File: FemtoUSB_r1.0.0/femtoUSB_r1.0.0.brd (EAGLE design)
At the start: 20.7 x 15.2 mm, 25 parts, among them IC1 ATSAMD21E18A-MUT

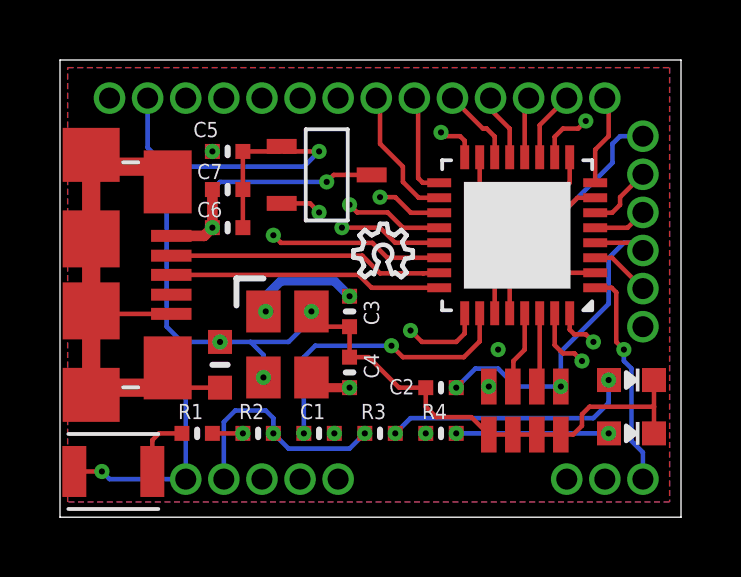
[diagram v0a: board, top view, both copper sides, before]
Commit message: Corrected the Make and model of the LDO Voltage Regulator. Board now powers on.
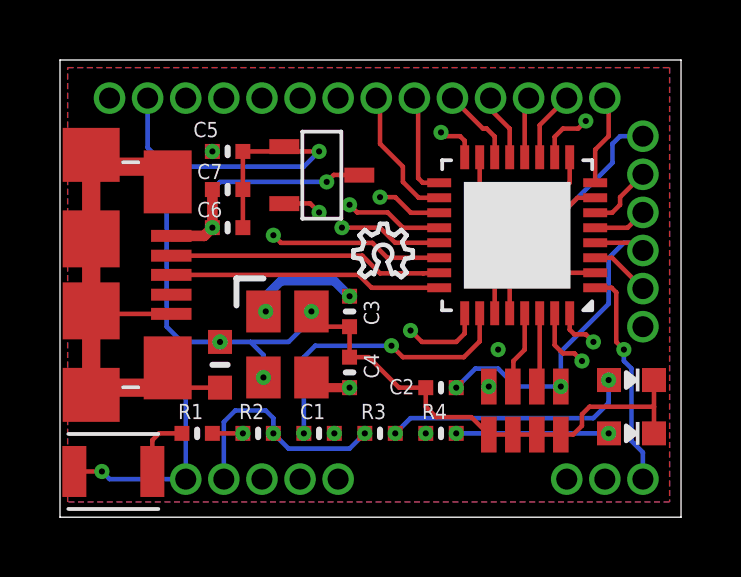
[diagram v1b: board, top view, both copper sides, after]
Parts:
- LDO_VREG: value LM3480 -> MCP1700T-3302E/TT; device ti-lm3480:LM3480 -> MCP1700T-3302E_TT:MCP1700T-3302E/TT
- moved LDO_VREG 1.64 mm to (8.08, 12.9)
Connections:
- net 3.3V: now also LDO_VREG.VOUT; no longer LDO_VREG.P$2
- net GND: now also LDO_VREG.GND; no longer LDO_VREG.P$1
- net VIN: now also LDO_VREG.VIN; no longer LDO_VREG.P$3
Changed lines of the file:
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@@
 <setting verticaltext="up"/>
 </settings>
-<grid distance="10" unitdist="mil" unit="mil" style="lines" multiple="1" display="yes" altdistance="0.025" altunitdist="inch" altunit="inch"/>
+<grid distance="1" unitdist="mil" unit="mil" style="lines" multiple="1" display="yes" altdistance="0.025" altunitdist="inch" altunit="inch"/>
 <layers>
 <layer number="1" name="Top" color="4" fill="1" visible="yes" active="yes"/>
@@
 <attribute name="DIGIKEY_PART" value="TSX-3225 32.0000MF15X-B-ND" x="8.382" y="6.858" size="1.778" layer="27" rot="R270" display="off"/>
 </element>
-<element name="LDO_VREG" library="ti-lm3480" package="LM3480" value="LM3480" x="8.89" y="11.43" rot="R270"/>
+<element name="LDO_VREG" library="MCP1700T-3302E_TT" package="MCP1700T-3302E/TT" value="MCP1700T-3302E/TT" x="8.0772" y="12.8524" rot="R270"/>
 <element name="C5" library="microbuilder" package="_0402MP" value="2.2uF" x="5.588" y="12.192" smashed="yes">
 <attribute name="NAME" x="4.445" y="12.6683" size="0.508" layer="25" font="vector" ratio="20"/>
@@
 <contactref element="C4" pad="1"/>
 <contactref element="LED1" pad="C"/>
-<contactref element="LDO_VREG" pad="P$1"/>
+<contactref element="LDO_VREG" pad="GND"/>
 <contactref element="C5" pad="2"/>
 <contactref element="C6" pad="2"/>
@@
 <wire x1="6.096" y1="12.192" x2="6.096" y2="10.922" width="0.1524" layer="1"/>
 <wire x1="6.096" y1="12.192" x2="7.304" y2="12.192" width="0.1524" layer="1"/>
-<wire x1="7.304" y1="12.192" x2="7.39" y2="12.36" width="0.1524" layer="1"/>
+<wire x1="7.304" y1="12.192" x2="7.4772" y2="12.3524" width="0.1524" layer="1"/>
 <wire x1="2.921" y1="13.97" x2="2.921" y2="12.319" width="0.1524" layer="16"/>
 <wire x1="2.921" y1="12.319" x2="3.556" y2="11.684" width="0.1524" layer="16"/>
@@
 <via x="8.636" y="12.192" extent="1-16" drill="0.2032" diameter="0.508"/>
 <wire x1="8.636" y1="12.192" x2="7.476" y2="12.192" width="0.1524" layer="1"/>
-<wire x1="7.476" y1="12.192" x2="7.39" y2="12.36" width="0.1524" layer="1"/>
+<wire x1="7.476" y1="12.192" x2="7.4772" y2="12.3524" width="0.1524" layer="1"/>
 <wire x1="0.478" y1="1.524" x2="1.397" y2="1.524" width="0.1524" layer="1"/>
 <via x="1.397" y="1.524" extent="1-16" drill="0.2032" diameter="0.508"/>
@@
 <contactref element="C5" pad="1"/>
 <contactref element="R3" pad="1"/>
-<contactref element="LDO_VREG" pad="P$2"/>
+<contactref element="LDO_VREG" pad="VOUT"/>
 <via x="5.08" y="12.192" extent="1-16" drill="0.2032" diameter="0.508"/>
 <wire x1="5.08" y1="12.192" x2="4.318" y2="12.954" width="0.1524" layer="15"/>
@@
 <wire x1="6.096" y1="9.652" x2="7.112" y2="10.668" width="0.1524" layer="15"/>
 <via x="10.16" y="2.794" extent="1-16" drill="0.2032" diameter="0.508"/>
-<wire x1="7.39" y1="10.46" x2="8.336" y2="10.46" width="0.1524" layer="1"/>
+<wire x1="7.4772" y1="10.4524" x2="8.336" y2="10.46" width="0.1524" layer="1"/>
 <wire x1="8.336" y1="10.46" x2="8.636" y2="10.16" width="0.1524" layer="1"/>
 <wire x1="7.112" y1="2.794" x2="7.62" y2="2.286" width="0.1524" layer="16"/>
@@
 <wire x1="1.524" y1="12.446" x2="1.524" y2="13.843" width="0.1524" layer="15"/>
 <wire x1="1.524" y1="13.843" x2="1.651" y2="13.97" width="0.1524" layer="15"/>
-<contactref element="LDO_VREG" pad="P$3"/>
+<contactref element="LDO_VREG" pad="VIN"/>
 <contactref element="C6" pad="1"/>
 <contactref element="C7" pad="1"/>
@@
 <wire x1="5.334" y1="11.176" x2="5.08" y2="10.922" width="0.1524" layer="16"/>
 <wire x1="5.08" y1="10.922" x2="5.08" y2="9.652" width="0.1524" layer="16"/>
-<wire x1="10.39" y1="11.41" x2="9.124" y2="11.41" width="0.1524" layer="1"/>
+<wire x1="9.9772" y1="11.4024" x2="9.124" y2="11.41" width="0.1524" layer="1"/>
 <wire x1="9.124" y1="11.41" x2="8.89" y2="11.176" width="0.1524" layer="1"/>
 </signal>

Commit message: Updating the QFN (no leads) chip version of the board - adding in missing 10uF caps and 10uH inductor
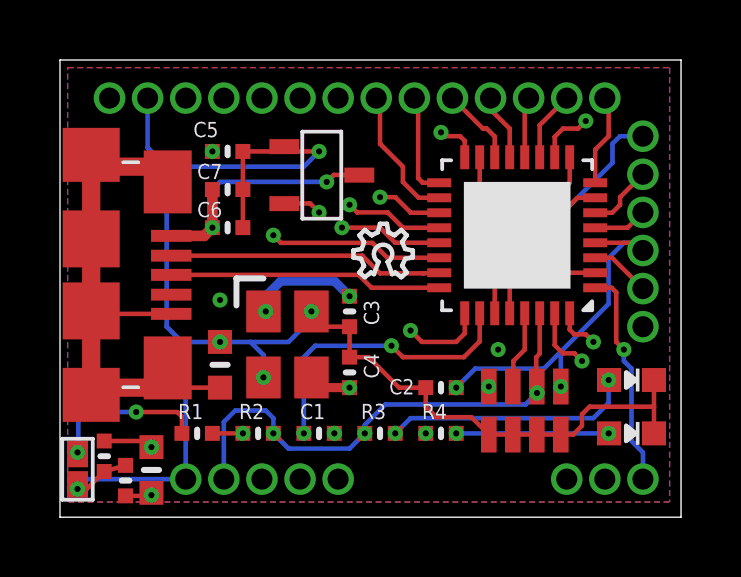
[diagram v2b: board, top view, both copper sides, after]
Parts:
- added C8, C9: 10uF, microbuilder:_0402MP
- added L1: 10uH, microbuilder:_0603MP
- BTN: device omron_tactile_switch:SIDE_ACT_NO_GND_NO_BOSS -> femtoduino:SPST_SMD
- moved BTN 1.20 mm to (0.58, 1.60), turned to 270 degrees
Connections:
- removed net VDDIN: C_ARR1.5, IC1.30
- net 3.3V: now also C8.2, C_ARR1.5, IC1.30, L1.1
- net GND: now also C8.1, C9.1
- net VDDANA: now also C9.2, L1.2
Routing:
- net 3.3V: track 25.1 -> 40.0 mm, vias 4 -> 7
- net VDDANA: track 9.06 -> 23.8 mm, vias 2 -> 3
- net N$26: track 2.12 -> 5.30 mm, vias 0 -> 2
- net VDDIN: track 2.48 -> 0.00 mm
- net GND: track 70.4 -> 72.4 mm
- net PA28: track 11.2 -> 12.3 mm

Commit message: Updating r1.x version of FemtoUSB (QFN and QFP chip version). Pin PA15 and GND pads now available to start board up in bootloader mode (SAM-BA)
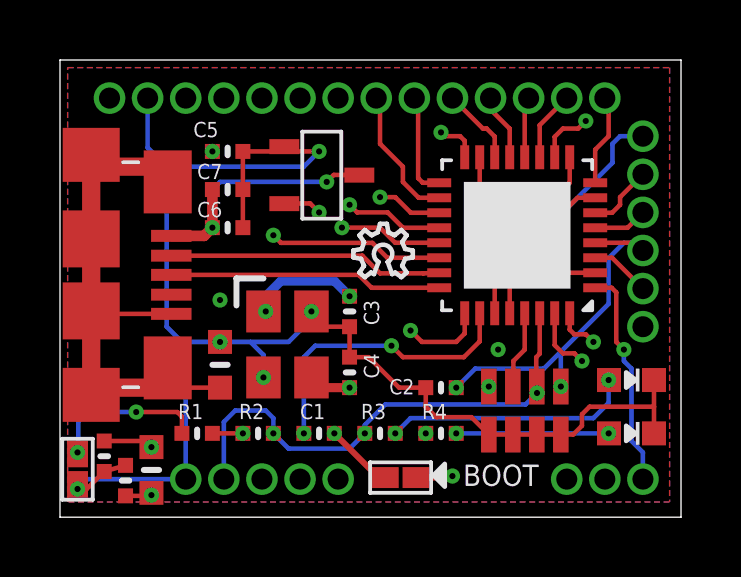
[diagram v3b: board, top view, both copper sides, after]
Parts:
- added U$38: SPST_SMD, femtoduino:SPST_SMD
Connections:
- net GND: now also U$38.2
- net PA15/XOUT: now also U$38.1
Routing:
- net PA15/XOUT: track 13.1 -> 21.7 mm, vias 2 -> 3
- net GND: track 72.4 -> 74.7 mm
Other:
- board text added: "BOOT"
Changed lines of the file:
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@@
 <setting verticaltext="up"/>
 </settings>
-<grid distance="1" unitdist="mil" unit="mil" style="lines" multiple="1" display="yes" altdistance="0.025" altunitdist="inch" altunit="inch"/>
+<grid distance="5" unitdist="mil" unit="mil" style="lines" multiple="1" display="yes" altdistance="0.025" altunitdist="inch" altunit="inch"/>
 <layers>
 <layer number="1" name="Top" color="4" fill="1" visible="yes" active="yes"/>
@@
 <wire x1="0" y1="15.24" x2="0" y2="0" width="0" layer="20"/>
 <text x="3.429" y="4.826" size="0.7112" layer="26" font="vector" ratio="20" rot="MR90">FemtoUSB</text>
-<text x="2.159" y="5.715" size="0.7112" layer="26" font="vector" ratio="20" rot="MR90">r1.0.0</text>
+<text x="2.0828" y="6.6548" size="0.7112" layer="26" font="vector" ratio="20" rot="MR90">r1.0.0</text>
 <text x="0.762" y="3.175" size="0.7112" layer="26" font="vector" ratio="20" rot="MR90">femtoduino.com</text>
 <text x="2.032" y="13.081" size="0.7112" layer="26" font="vector" ratio="20" rot="SMR90" align="top-right">VIN</text>
@@
 <circle x="16.2814" y="6.5786" radius="0.250159375" width="0.254" layer="26"/>
 <circle x="16.2814" y="5.5626" radius="0.250159375" width="0.254" layer="26"/>
+<text x="13.4366" y="1.0414" size="0.7112" layer="25" font="vector" ratio="20">BOOT</text>
+<polygon width="0.1524" layer="25">
+<vertex x="12.827" y="1.778"/>
+<vertex x="12.446" y="1.397"/>
+<vertex x="12.827" y="1.016"/>
+</polygon>
 </plain>
 <attributes>
@@
 <element name="C9" library="microbuilder" package="_0402MP" value="10uF" x="1.4732" y="2.032" smashed="yes" rot="R90"/>
 <element name="C8" library="microbuilder" package="_0402MP" value="10uF" x="2.1844" y="1.2192" smashed="yes" rot="R270"/>
+<element name="U$38" library="femtoduino" package="SPST_SMD" value="SPST_SMD" x="11.3538" y="1.3208" rot="R180"/>
 </elements>
 <signals>
@@
 <wire x1="11.43" y1="7.874" x2="9.652" y2="6.096" width="0.1524" layer="15"/>
 <wire x1="9.652" y1="6.096" x2="9.652" y2="4.318" width="0.1524" layer="15"/>
+<contactref element="U$38" pad="1"/>
+<wire x1="11.8618" y1="1.3208" x2="13.0302" y2="1.3208" width="0.2032" layer="1"/>
+<wire x1="13.0302" y1="1.3208" x2="13.081" y2="1.3716" width="0.2032" layer="1"/>
+<via x="13.081" y="1.3716" extent="1-16" drill="0.2032" diameter="0.508"/>
+<wire x1="13.081" y1="1.3716" x2="13.6652" y2="1.3716" width="0.1524" layer="2"/>
+<wire x1="13.6652" y1="1.3716" x2="14.1478" y2="1.8542" width="0.1524" layer="2"/>
+<wire x1="14.1478" y1="1.8542" x2="14.1478" y2="2.9464" width="0.1524" layer="2"/>
+<wire x1="14.1478" y1="2.9464" x2="13.7922" y2="3.302" width="0.1524" layer="2"/>
+<wire x1="13.7922" y1="3.302" x2="10.668" y2="3.302" width="0.1524" layer="2"/>
+<wire x1="10.668" y1="3.302" x2="9.652" y2="4.318" width="0.1524" layer="2"/>
 </signal>
 <signal name="PA16/SERCOM1/PAD[0]/SPI/I2C">
@@
 <wire x1="12.192" y1="5.842" x2="12.192" y2="4.318" width="0.1524" layer="2"/>
 <wire x1="12.192" y1="4.318" x2="12.827" y2="3.683" width="0.1524" layer="2"/>
-<wire x1="12.827" y1="3.683" x2="13.462" y2="3.683" width="0.1524" layer="2"/>
-<wire x1="13.462" y1="3.683" x2="13.97" y2="3.175" width="0.1524" layer="2"/>
-<wire x1="13.97" y1="3.175" x2="14.986" y2="3.175" width="0.1524" layer="2"/>
-<wire x1="14.986" y1="3.175" x2="16.891" y2="1.27" width="0.1524" layer="2"/>
+<wire x1="12.827" y1="3.683" x2="14.478" y2="3.683" width="0.1524" layer="2"/>
+<wire x1="14.478" y1="3.683" x2="16.891" y2="1.27" width="0.1524" layer="2"/>
 </signal>
 <signal name="RESET">
@@
 <wire x1="0.889" y1="0.9398" x2="0.5842" y2="0.9398" width="0.1524" layer="1"/>
 <wire x1="1.4732" y1="1.524" x2="2.1844" y2="1.7272" width="0.1524" layer="1"/>
+<contactref element="U$38" pad="2"/>
+<wire x1="10.8458" y1="1.3208" x2="10.6172" y2="1.3208" width="0.2032" layer="1"/>
+<wire x1="10.6172" y1="1.3208" x2="9.144" y2="2.794" width="0.2032" layer="1"/>
 </signal>
 <signal name="3.3V">
@@
 <wire x1="3.048" y1="0.7366" x2="2.9464" y2="0.7112" width="0.1524" layer="1"/>
 <wire x1="2.9464" y1="0.7112" x2="2.1844" y2="0.7112" width="0.1524" layer="1"/>
+<wire x1="3.048" y1="0.7366" x2="3.048" y2="0.8128" width="0" layer="19" extent="1-2"/>
 </signal>
 <signal name="N$32">

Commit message: Updating gerbers and BoM/Partslist of QFN version
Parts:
- EPSON_TSX1: value 32MHz -> 48MHz
- LED1: value RED -> YELLOW
- LED2: value GREEN -> BLUE
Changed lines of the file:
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@@
 <attribute name="VALUE" x="8.001" y="2.0002" size="0.4572" layer="27" font="vector" ratio="20"/>
 </element>
-<element name="LED1" library="microbuilder" package="CHIPLED_0603_NOOUTLINE" value="RED" x="19.05" y="4.572" smashed="yes" rot="R270"/>
+<element name="LED1" library="microbuilder" package="CHIPLED_0603_NOOUTLINE" value="YELLOW" x="19.05" y="4.572" smashed="yes" rot="R270"/>
 <element name="R1" library="microbuilder" package="_0402MP" value="330" x="4.572" y="2.794" smashed="yes">
 <attribute name="NAME" x="3.937" y="3.2703" size="0.508" layer="25" font="vector" ratio="20"/>
@@
 <attribute name="NAME" x="10.1283" y="5.461" size="0.508" layer="25" font="vector" ratio="20" rot="R270"/>
 </element>
-<element name="LED2" library="microbuilder" package="CHIPLED_0603_NOOUTLINE" value="GREEN" x="19.05" y="2.794" smashed="yes" rot="R270"/>
+<element name="LED2" library="microbuilder" package="CHIPLED_0603_NOOUTLINE" value="BLUE" x="19.05" y="2.794" smashed="yes" rot="R270"/>
 <element name="R2" library="microbuilder" package="_0402MP" value="10K" x="6.604" y="2.794" smashed="yes">
 <attribute name="NAME" x="5.969" y="3.2703" size="0.508" layer="25" font="vector" ratio="20"/>
@@
 </element>
 <element name="BTN" library="femtoduino" package="SPST_SMD" value="OMRON B3U-300P(M)" x="0.5842" y="1.6002" rot="R270"/>
-<element name="EPSON_TSX1" library="crystals" package="TSX-3225" value="32MHz" x="8.382" y="6.858" smashed="yes" rot="R270">
+<element name="EPSON_TSX1" library="crystals" package="TSX-3225" value="48MHz" x="8.382" y="6.858" smashed="yes" rot="R270">
 <attribute name="DIGIKEY_PART" value="TSX-3225 32.0000MF15X-B-ND" x="8.382" y="6.858" size="1.778" layer="27" rot="R270" display="off"/>
 </element>
@@
 <wire x1="3.048" y1="0.7366" x2="2.9464" y2="0.7112" width="0.1524" layer="1"/>
 <wire x1="2.9464" y1="0.7112" x2="2.1844" y2="0.7112" width="0.1524" layer="1"/>
-<wire x1="3.048" y1="0.7366" x2="3.048" y2="0.8128" width="0" layer="19" extent="1-2"/>
+<wire x1="3.048" y1="0.8128" x2="3.048" y2="0.7366" width="0.1524" layer="1"/>
 </signal>
 <signal name="N$32">
